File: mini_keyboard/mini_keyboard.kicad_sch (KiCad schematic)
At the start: 46 parts, among them U1 MX1A-11NN, U10 MX1A-11NN, U100 DEV-15583, U101 ABX00027, U11 MX1A-11NN, U12 MX1A-11NN, U13 MX1A-11NN, U14 MX1A-11NN, U15 MX1A-11NN, U16 MX1A-11NN, U17 MX1A-11NN, U18 MX1A-11NN, U19 MX1A-11NN, U2 MX1A-11NN, U20 MX1A-11NN, U21 MX1A-11NN, U22 MX1A-11NN, U23 MX1A-11NN, U24 MX1A-11NN, U25 MX1A-11NN, U26 MX1A-11NN, U27 MX1A-11NN, U29 MX1A-11NN, U3 MX1A-11NN, U30 MX1A-11NN, U31 MX1A-11NN, U32 MX1A-11NN, U33 MX1A-11NN, U34 MX1A-11NN, U36 MX1A-11NN, U37 MX1A-11NN, U38 MX1A-11NN, U39 MX1A-11NN, U4 MX1A-11NN, U5 MX1A-11NN, U6 MX1A-11NN, U7 MX1A-11NN, U8 MX1A-11NN, U9 MX1A-11NN

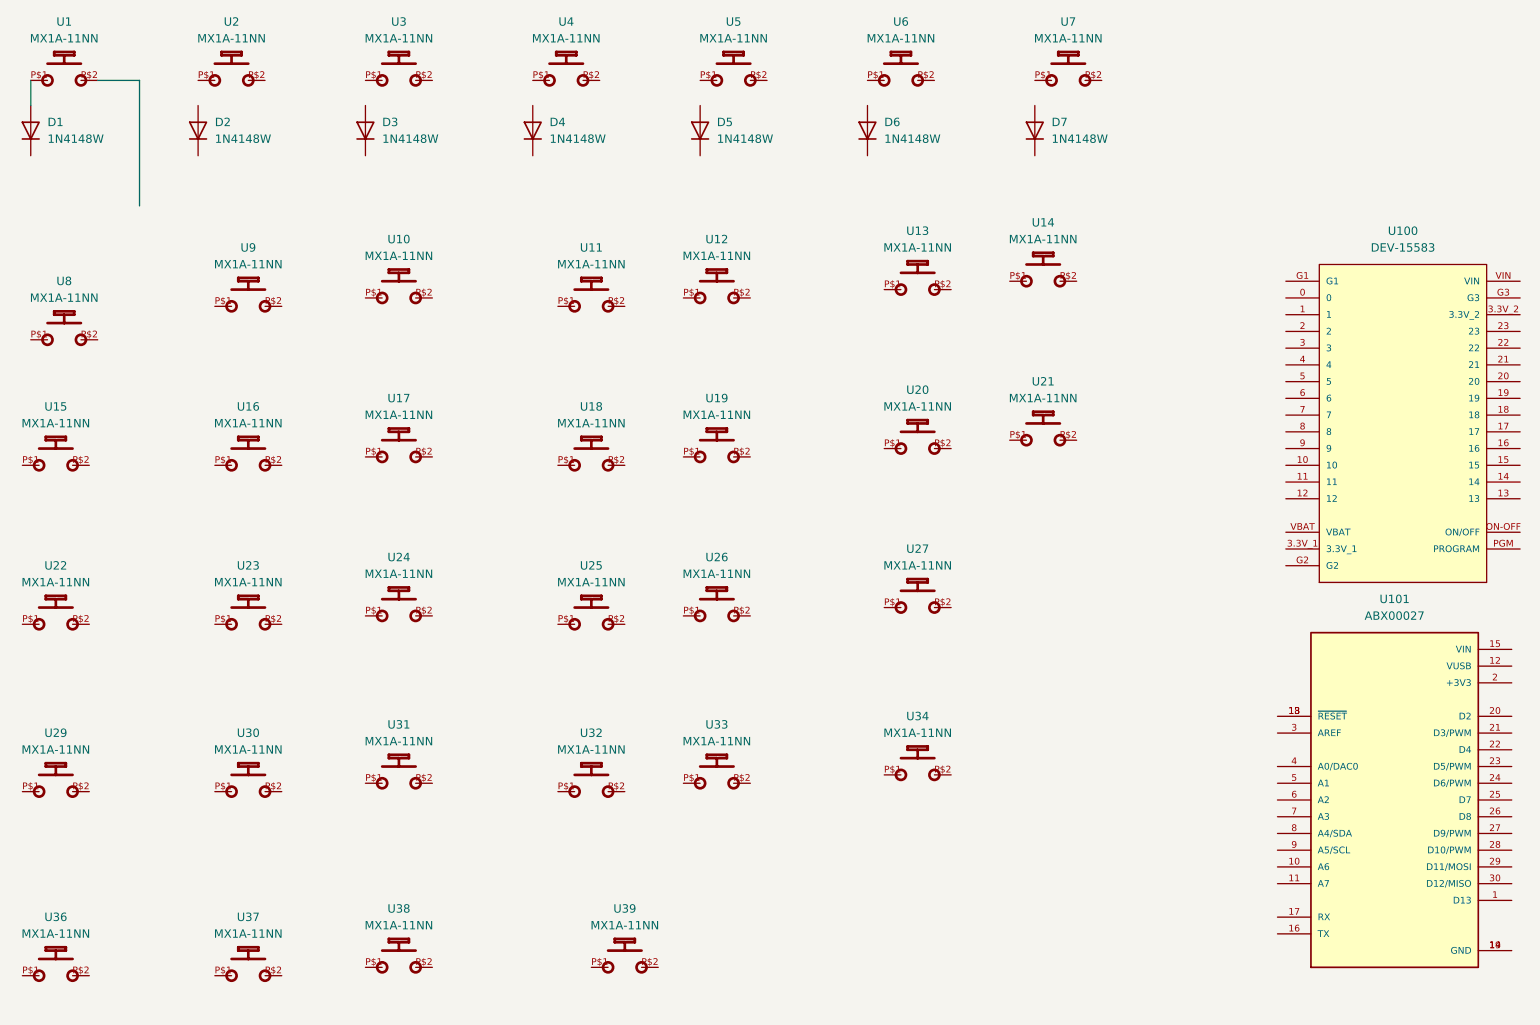
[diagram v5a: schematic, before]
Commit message: initial placement of all diodes
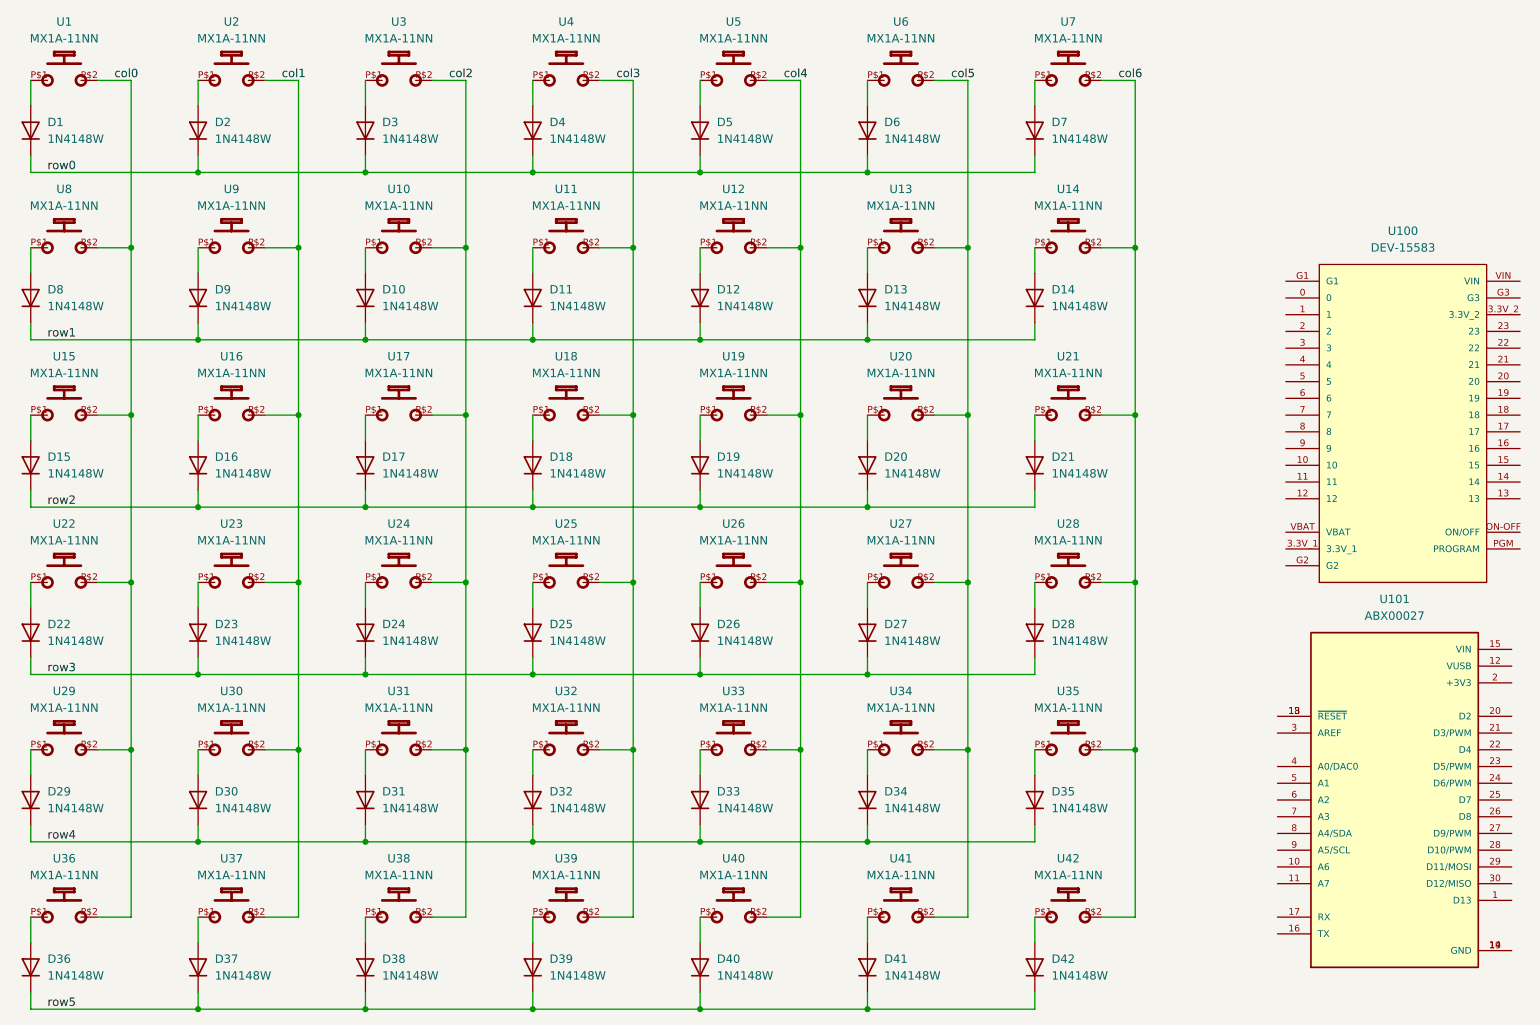
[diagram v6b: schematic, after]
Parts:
- added D10, D11, D12, D13, D14, D15, D16, D17, D18, D19, D20, D21, D22, D23, D24, D25, D26, D27, D28, D29, D30, D31, D32, D33, D34, D35, D36, D37, D38, D39, D40, D41, D42, D8, D9: 1N4148W, Diode_SMD:D_SOD-123, symbol Diode:1N4148W
- added U28, U35, U40, U41, U42: MX1A-11NN, pedrolib:CHERRY_MX1A-11NN_SWITCH, symbol pedrolib:MX1A-11NN
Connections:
- net row0: now reaches D3.1 (K)
- net row0: now also D1.1 (K), D2.1 (K), D4.1 (K), D5.1 (K), D6.1 (K), D7.1 (K)
- net at D3.2 (A): now also U3.P$1
- net at U27.P$1: now also D27.2 (A)
- net col5: now reaches U27.P$2
- net col5: now also U13.P$2, U20.P$2, U34.P$2, U6.P$2, U41.P$2
- net at U18.P$1: now also D18.2 (A)
- net col3: now reaches U18.P$2
- net col3: now also U11.P$2, U25.P$2, U32.P$2, U39.P$2, U4.P$2
- net at U38.P$1: now also D38.2 (A)
- net col2: now reaches U38.P$2
- net col2: now also U10.P$2, U17.P$2, U24.P$2, U3.P$2, U31.P$2
- net at D6.2 (A): now also U6.P$1
- net at U29.P$1: now also D29.2 (A)
- net col0: now reaches U29.P$2
- net col0: now also U1.P$2, U15.P$2, U22.P$2, U36.P$2, U8.P$2
- net at D5.2 (A): now also U5.P$1
- net at U30.P$1: now also D30.2 (A)
- net col1: now reaches U30.P$2
- net col1: now also U16.P$2, U2.P$2, U23.P$2, U37.P$2, U9.P$2
- net at U13.P$1: now also D13.2 (A)
- net col4: now reaches U5.P$2
- net col4: now also U12.P$2, U19.P$2, U26.P$2, U33.P$2, U40.P$2
- net at U23.P$1: now also D23.2 (A)
- net at U14.P$1: now also D14.2 (A)
- net col6: now reaches U14.P$2
- net col6: now also U21.P$2, U7.P$2, U28.P$2, U35.P$2, U42.P$2
- net at U20.P$1: now also D20.2 (A)
- net at U8.P$1: now also D8.2 (A)
- net at U22.P$1: now also D22.2 (A)
- net at D2.2 (A): now also U2.P$1
- net at U33.P$1: now also D33.2 (A)
- net at U17.P$1: now also D17.2 (A)
- net at U19.P$1: now also D19.2 (A)
- net at U36.P$1: now also D36.2 (A)
- net at U39.P$1: now also D39.2 (A)
- net at U34.P$1: now also D34.2 (A)
- net at U7.P$1: now also D7.2 (A)
- net at D4.2 (A): now also U4.P$1
- net at U15.P$1: now also D15.2 (A)
- net at U9.P$1: now also D9.2 (A)
- net at U24.P$1: now also D24.2 (A)
- net at U25.P$1: now also D25.2 (A)
- net at U37.P$1: now also D37.2 (A)
- net at U32.P$1: now also D32.2 (A)
- net at U26.P$1: now also D26.2 (A)
- net at U16.P$1: now also D16.2 (A)
- net at U11.P$1: now also D11.2 (A)
- net at U21.P$1: now also D21.2 (A)
- net at U31.P$1: now also D31.2 (A)
- net at U10.P$1: now also D10.2 (A)
- net at U12.P$1: now also D12.2 (A)
- new net: D40.2 (A), U40.P$1
- new net: D35.2 (A), U35.P$1
- new net: D41.2 (A), U41.P$1
- new net: D42.2 (A), U42.P$1
- new net: D28.2 (A), U28.P$1
- new net row1: D10.1 (K), D11.1 (K), D12.1 (K), D13.1 (K), D14.1 (K), D8.1 (K), D9.1 (K)
- new net row2: D15.1 (K), D16.1 (K), D17.1 (K), D18.1 (K), D19.1 (K), D20.1 (K), D21.1 (K)
- new net row3: D22.1 (K), D23.1 (K), D24.1 (K), D25.1 (K), D26.1 (K), D27.1 (K), D28.1 (K)
- new net row4: D29.1 (K), D30.1 (K), D31.1 (K), D32.1 (K), D33.1 (K), D34.1 (K), D35.1 (K)
- new net row5: D36.1 (K), D37.1 (K), D38.1 (K), D39.1 (K), D40.1 (K), D41.1 (K), D42.1 (K)
